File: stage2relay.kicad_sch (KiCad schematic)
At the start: 5 parts, among them SW2 SW_Push

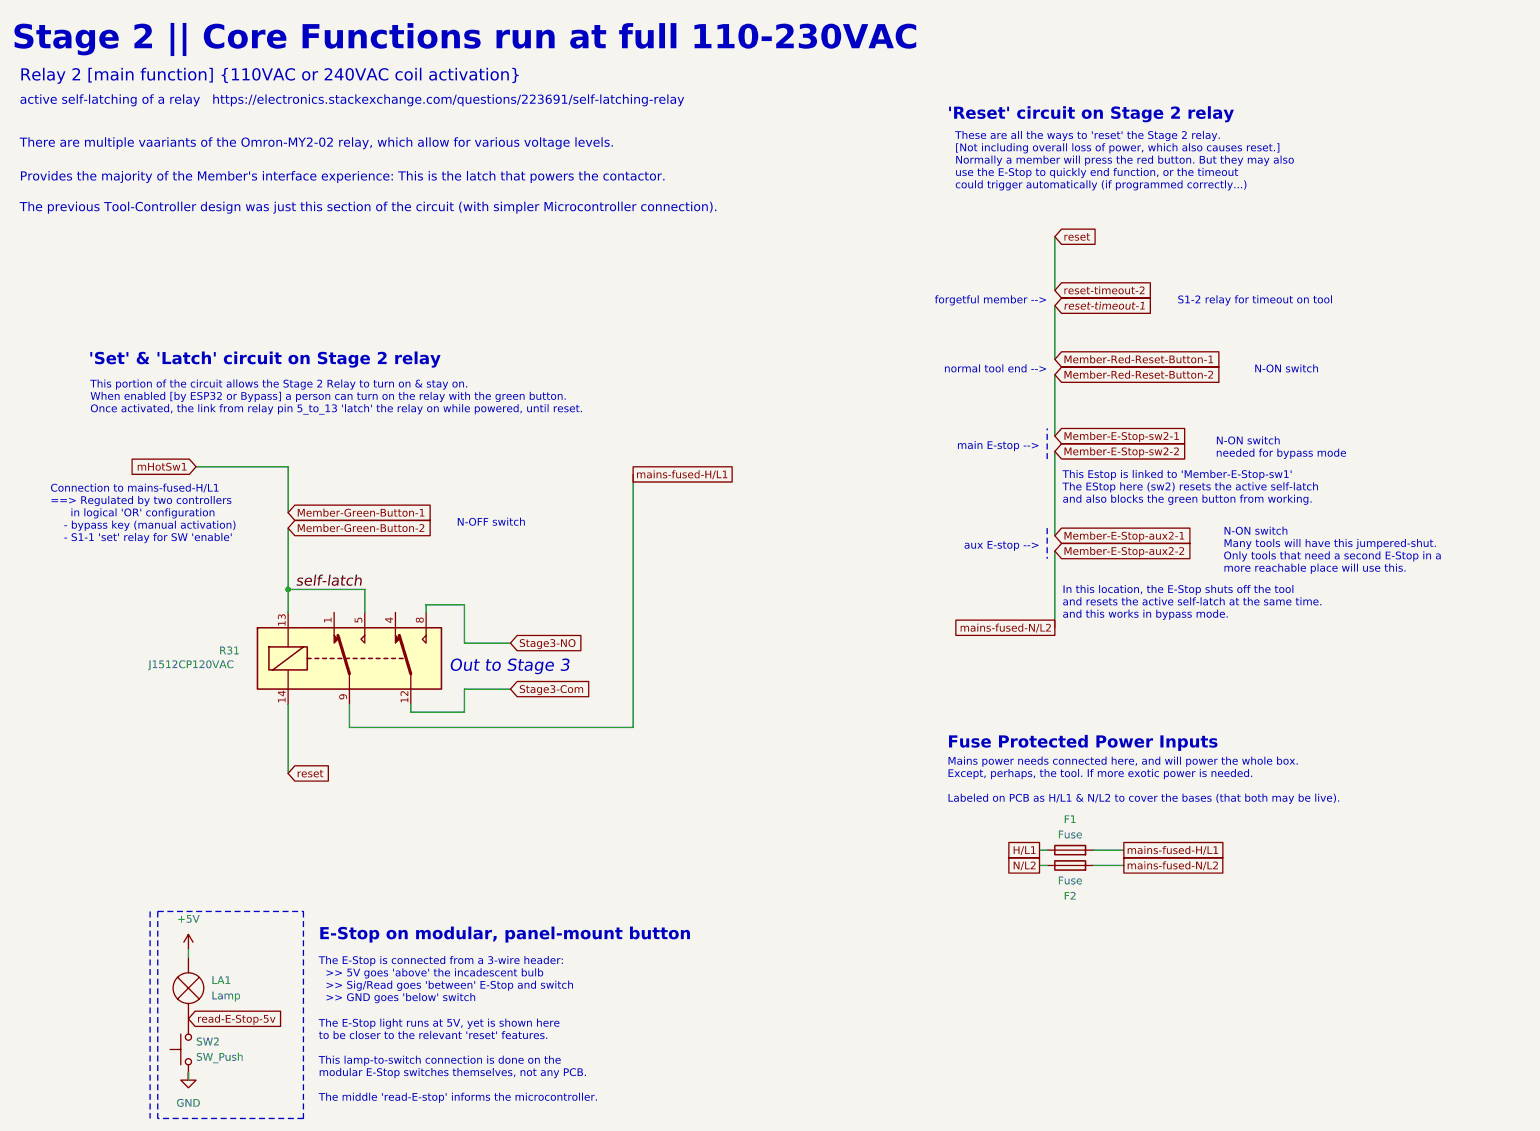
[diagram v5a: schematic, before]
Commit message: moved LED GPIO to fit free pins for ethernet wing
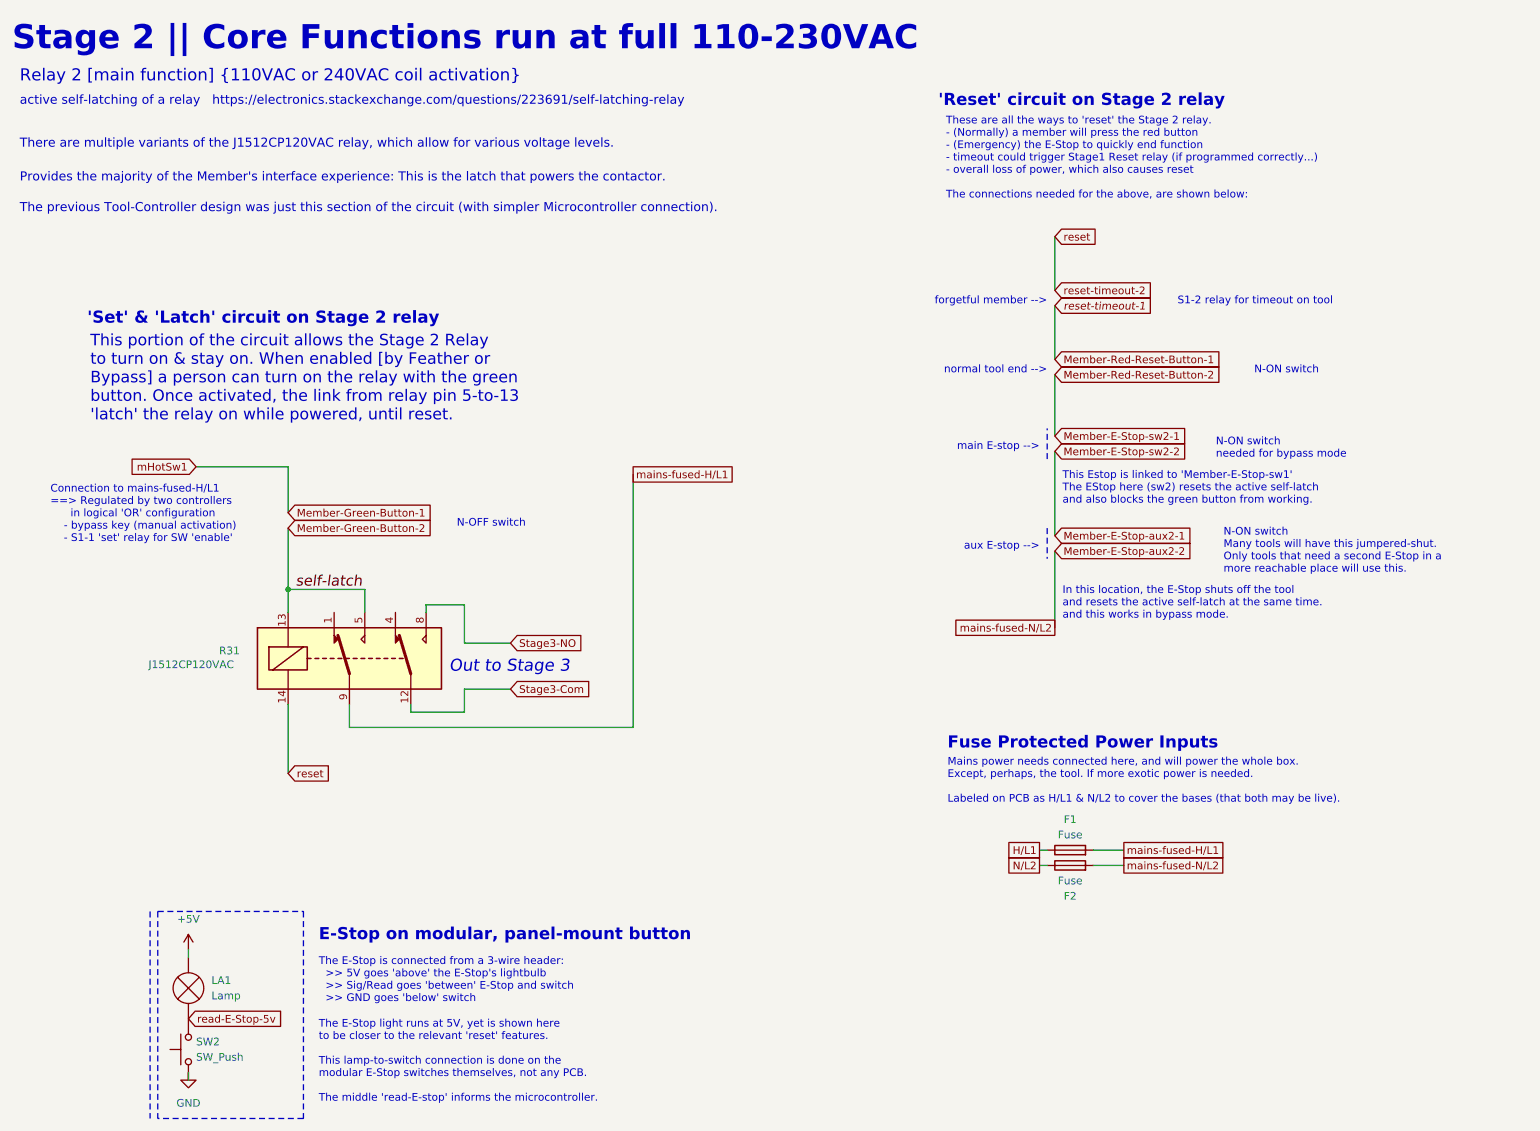
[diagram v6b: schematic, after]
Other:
- note added: "The E-Stop is connected from a 3-wire header: >> 5V goes 'above' the E-Stop's lightbulb >> Sig/Read goes 'between' E-Stop and switch >> GND goes 'below' switch"
- note added: "There are multiple variants of the J1512CP120VAC relay, which allow for various voltage levels."
- note added: "These are all the ways to 'reset' the Stage 2 relay. - (Normally) a member will press the red button - (Emergency) the E-Stop to quickly end function - timeout could trigger Stage1 Reset relay (if programmed correctly...) - overall loss of power, which also causes reset The connections needed for the above, are shown below:"
- note added: "This portion of the circuit allows the Stage 2 Relay to turn on & stay on. When enabled [by Feather or Bypass] a person can turn on the relay with the green button. Once activated, the link from relay pin 5-to-13 'latch' the relay on while powered, until reset."
- note removed: "The E-Stop is connected from a 3-wire header: >> 5V goes 'above' the incadescent bulb >> Sig/Read goes 'between' E-Stop and switch >> GND goes 'below' switch"
- note removed: "There are multiple vaariants of the Omron-MY2-02 relay, which allow for various voltage levels."
- note removed: "These are all the ways to 'reset' the Stage 2 relay. [Not including overall loss of power, which also causes reset.] Normally a member will press the red button. But they may also use the E-Stop to quickly end function, or the timeout could trigger automatically (if programmed correctly...)"
- note removed: "This portion of the circuit allows the Stage 2 Relay to turn on & stay on. When enabled [by ESP32 or Bypass] a person can turn on the relay with the green button. Once activated, the link from relay pin 5_to_13 'latch' the relay on while powered, until reset."
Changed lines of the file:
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@@
 	(text "'Reset' circuit on Stage 2 relay"
 		(exclude_from_sim no)
-		(at 175.26 33.02 0)
+		(at 173.736 30.734 0)
 		(effects
 			(font
@@
 		)
 	)
-	(text "There are multiple vaariants of the Omron-MY2-02 relay, which allow for various voltage levels."
+	(text "There are multiple variants of the J1512CP120VAC relay, which allow for various voltage levels."
 		(exclude_from_sim no)
 		(at 21.59 37.592 0)
@@
 		)
 	)
-	(text "The E-Stop is connected from a 3-wire header:\n  >> 5V goes 'above' the incadescent bulb\n  >> Sig/Read goes 'between' E-Stop and switch\n  >> GND goes 'below' switch"
+	(text "The E-Stop is connected from a 3-wire header:\n  >> 5V goes 'above' the E-Stop's lightbulb\n  >> Sig/Read goes 'between' E-Stop and switch\n  >> GND goes 'below' switch"
 		(exclude_from_sim no)
 		(at 71.12 179.07 0)
@@
 		)
 	)
-	(text "These are all the ways to 'reset' the Stage 2 relay. \n[Not including overall loss of power, which also causes reset.]\nNormally a member will press the red button. But they may also \nuse the E-Stop to quickly end function, or the timeout \ncould trigger automatically (if programmed correctly...)"
-		(exclude_from_sim no)
-		(at 176.53 44.45 0)
+	(text "These are all the ways to 'reset' the Stage 2 relay. \n- (Normally) a member will press the red button \n- (Emergency) the E-Stop to quickly end function\n- timeout could trigger Stage1 Reset relay (if programmed correctly...)\n- overall loss of power, which also causes reset\n\nThe connections needed for the above, are shown below:"
+		(exclude_from_sim no)
+		(at 175.006 45.974 0)
 		(effects
 			(font
@@
 			)
 			(justify left bottom)
+			(href "https://electronics.stackexchange.com/questions/223691/self-latching-relay")
 		)
 	)
@@
 	(text "'Set' & 'Latch' circuit on Stage 2 relay"
 		(exclude_from_sim no)
-		(at 33.02 73.66 0)
+		(at 32.766 66.802 0)
 		(effects
 			(font
@@
 		)
 	)
-	(text "This portion of the circuit allows the Stage 2 Relay to turn on & stay on.\nWhen enabled [by ESP32 or Bypass] a person can turn on the relay with the green button.\nOnce activated, the link from relay pin 5_to_13 'latch' the relay on while powered, until reset."
-		(exclude_from_sim no)
-		(at 33.274 81.534 0)
-		(effects
-			(font
-				(size 1.27 1.27)
-			)
-			(justify left bottom)
+	(text "This portion of the circuit allows the Stage 2 Relay \nto turn on & stay on. When enabled [by Feather or \nBypass] a person can turn on the relay with the green \nbutton. Once activated, the link from relay pin 5-to-13 \n'latch' the relay on while powered, until reset."
+		(exclude_from_sim no)
+		(at 33.274 82.804 0)
+		(effects
+			(font
+				(size 1.905 1.905)
+			)
+			(justify left bottom)

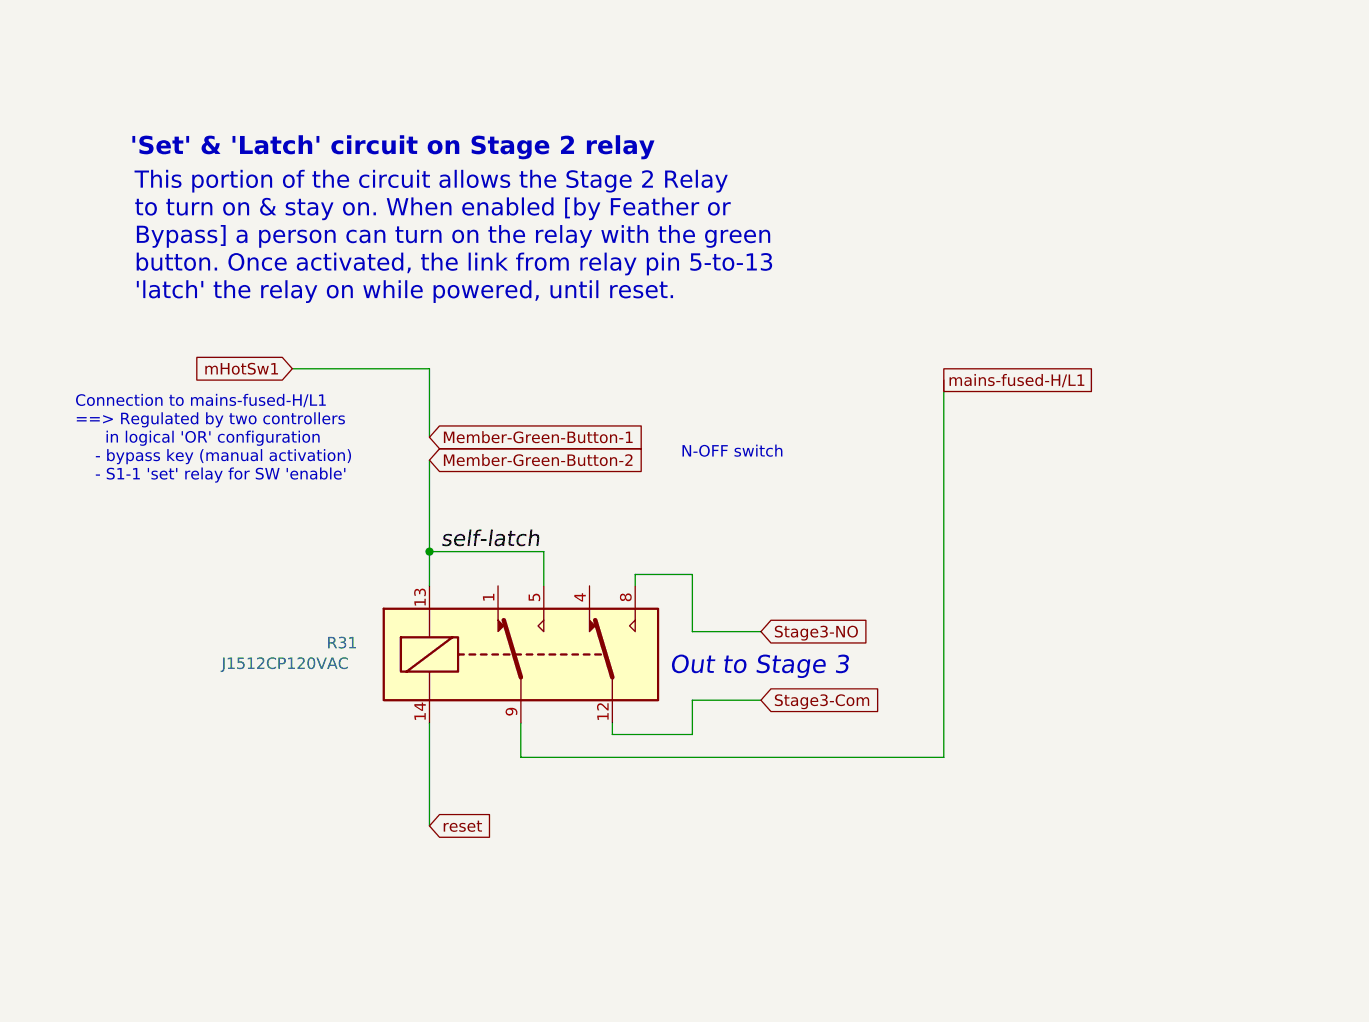
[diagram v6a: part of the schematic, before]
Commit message: changed to py14-02 relay socket
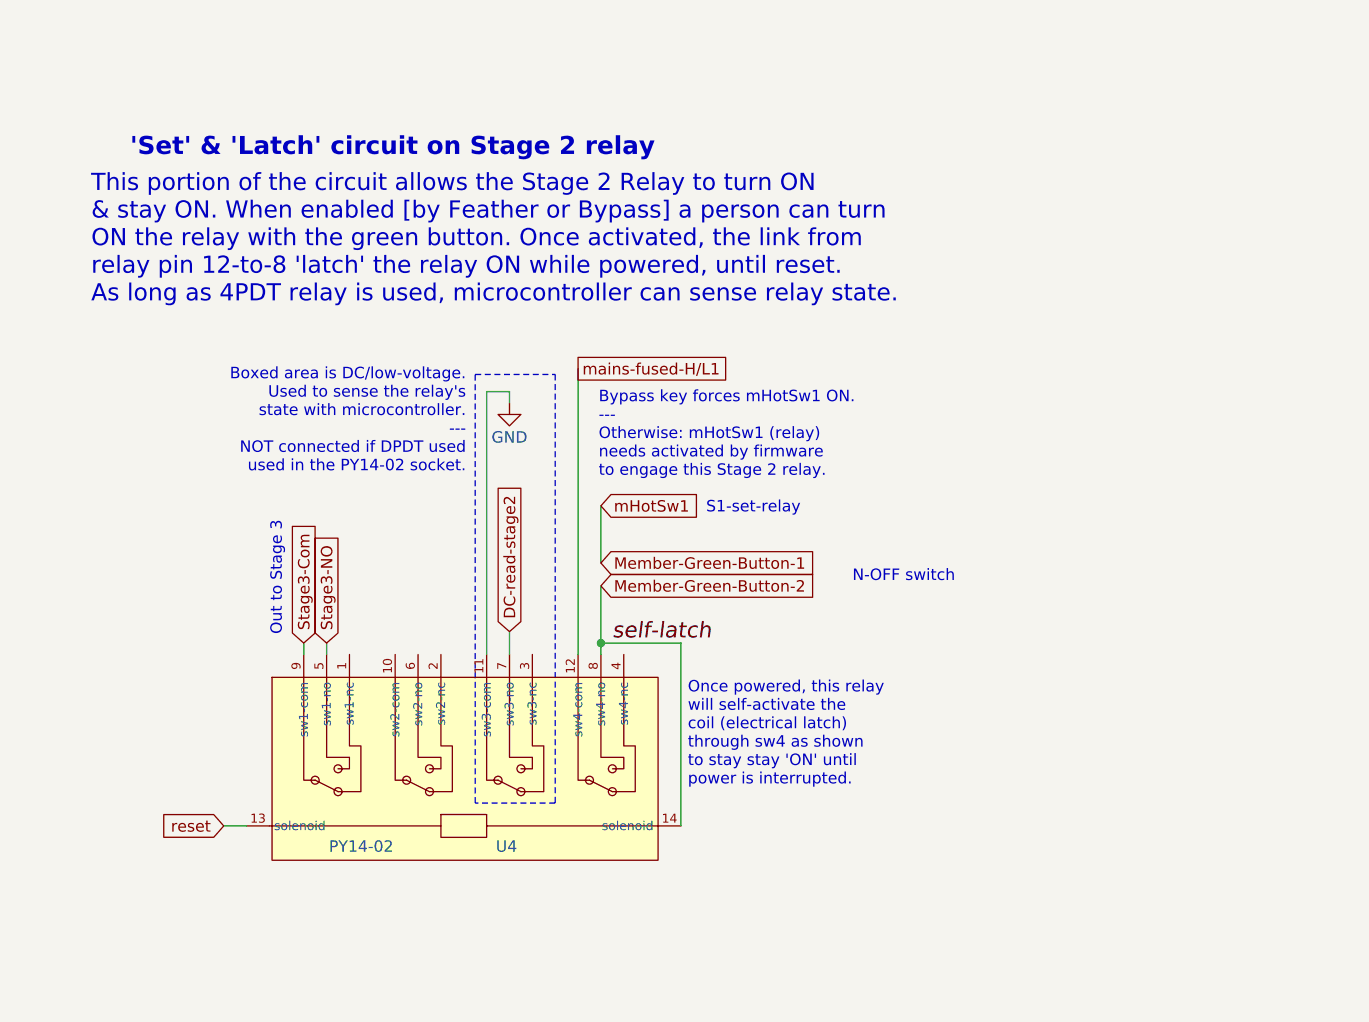
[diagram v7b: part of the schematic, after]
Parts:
- removed R31: J1512CP120VAC, j1512cp120vac1.2:relay-J1512CP120VAC, symbol Relay_Omron-MY2-02:Relay_Omron_MY2-02
- added U4: PY14-02, mk_relay_socket:RELAY-TH_PY14-02, symbol mk-relay-socket-14:PY14-02
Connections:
- net GND: now also U4.11 (sw3-com)
- net Member-Green-Button-2: now also U4.14 (solenoid), U4.8 (sw4-no)
- net Stage3-Com: now also U4.9 (sw1-com)
- net Stage3-NO: now also U4.5 (sw1-no)
- net mains-fused-H/L1: now also U4.12 (sw4-com)
- net reset: now also U4.13 (solenoid)
- new net DC-read-stage2: U4.7 (sw3-no)
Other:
- note added: "Boxed area is DC/low-voltage. Used to sense the relay's state with microcontroller. --- NOT connected if DPDT used used in the PY14-02 socket."
- note added: "Bypass key forces mHotSw1 ON. --- Otherwise: mHotSw1 (relay) needs activated by firmware to engage this Stage 2 relay."
- note added: "Once powered, this relay will self-activate the coil (electrical latch) through sw4 as shown to stay stay 'ON' until power is interrupted."
- note added: "S1-set-relay"
- note added: "This portion of the circuit allows the Stage 2 Relay to turn ON & stay ON. When enabled [by Feather or Bypass] a person can turn ON the relay with the green button. Once activated, the link from relay pin 12-to-8 'latch' the relay ON while powered, until reset. As long as 4PDT relay is used, microcontroller can sense relay state."
- note removed: "Connection to mains-fused-H/L1 ==> Regulated by two controllers in logical 'OR' configuration - bypass key (manual activation) - S1-1 'set' relay for SW 'enable'"
- note removed: "This portion of the circuit allows the Stage 2 Relay to turn on & stay on. When enabled [by Feather or Bypass] a person can turn on the relay with the green button. Once activated, the link from relay pin 5-to-13 'latch' the relay on while powered, until reset."
